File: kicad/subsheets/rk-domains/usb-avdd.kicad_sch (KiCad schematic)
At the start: 16 parts, among them U5 RK3566

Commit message: Mark as R1.0
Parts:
- renumbered C123 to C104, C122 to C105, C121 to C106, C124 to C107, C125 to C108, C155 to C109, C116 to C110, C117 to C111, C118 to C112, R44 to R38, R42 to R39, R43 to R40, R39 to R41, R40 to R42, R41 to R43
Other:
- company: (none) -> UVic Rocketry
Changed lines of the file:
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@@
 	(title_block
 		(title "USB AVDD")
+		(date "2025-11-23")
+		(rev "1.0")
+		(company "UVic Rocketry")
+		(comment 1 "Author: Eric Handley")
 	)
 	(junction
@@
 		(dnp no)
 		(fields_autoplaced yes)
-		(property "Reference" "#PWR062"
+		(property "Reference" "#PWR075"
 			(at 195.58 128.27 0)
 			(effects
@@
 			(project "srad-camera"
 				(path "/da62c771-e8c9-451f-8df1-ec995aadcb11/279fc251-45a8-41a3-8fcf-5855d7fe07da/ae41bc57-04fb-4570-b431-dc406bf562eb"
-					(reference "#PWR062")
+					(reference "#PWR075")
 					(unit 1)
 				)
@@
 		(dnp no)
 		(fields_autoplaced yes)
-		(property "Reference" "R44"
+		(property "Reference" "R38"
 			(at 215.9 62.23 90)
 			(effects
@@
 			(project "srad-camera"
 				(path "/da62c771-e8c9-451f-8df1-ec995aadcb11/279fc251-45a8-41a3-8fcf-5855d7fe07da/ae41bc57-04fb-4570-b431-dc406bf562eb"
-					(reference "R44")
+					(reference "R38")
 					(unit 1)
 				)
@@
 		(dnp no)
 		(fields_autoplaced yes)
-		(property "Reference" "C121"
+		(property "Reference" "C106"
 			(at 212.598 77.216 0)
 			(effects
@@
 			(project "srad-camera"
 				(path "/da62c771-e8c9-451f-8df1-ec995aadcb11/279fc251-45a8-41a3-8fcf-5855d7fe07da/ae41bc57-04fb-4570-b431-dc406bf562eb"
-					(reference "C121")
+					(reference "C106")
 					(unit 1)
 				)
@@
 		(dnp no)
 		(fields_autoplaced yes)
-		(property "Reference" "C117"
+		(property "Reference" "C111"
 			(at 107.188 117.348 0)
 			(effects
@@
 			(project "srad-camera"
 				(path "/da62c771-e8c9-451f-8df1-ec995aadcb11/279fc251-45a8-41a3-8fcf-5855d7fe07da/ae41bc57-04fb-4570-b431-dc406bf562eb"
-					(reference "C117")
+					(reference "C111")
 					(unit 1)
 				)
@@
 		(on_board yes)
 		(dnp no)
-		(property "Reference" "#PWR089"
+		(property "Reference" "#PWR074"
 			(at 81.28 101.6 0)
 			(effects
@@
 			(project "srad-camera"
 				(path "/da62c771-e8c9-451f-8df1-ec995aadcb11/279fc251-45a8-41a3-8fcf-5855d7fe07da/ae41bc57-04fb-4570-b431-dc406bf562eb"
-					(reference "#PWR089")
+					(reference "#PWR074")
 					(unit 1)
 				)
@@
 		(dnp no)
 		(fields_autoplaced yes)
-		(property "Reference" "#PWR061"
+		(property "Reference" "#PWR076"
 			(at 102.87 129.54 0)
 			(effects
@@
 			(project "srad-camera"
 				(path "/da62c771-e8c9-451f-8df1-ec995aadcb11/279fc251-45a8-41a3-8fcf-5855d7fe07da/ae41bc57-04fb-4570-b431-dc406bf562eb"
-					(reference "#PWR061")
+					(reference "#PWR076")
 					(unit 1)
 				)
@@
 		(on_board yes)
 		(dnp no)
-		(property "Reference" "C123"
+		(property "Reference" "C104"
 			(at 201.676 70.104 0)
 			(effects
@@
 			(project "srad-camera"
 				(path "/da62c771-e8c9-451f-8df1-ec995aadcb11/279fc251-45a8-41a3-8fcf-5855d7fe07da/ae41bc57-04fb-4570-b431-dc406bf562eb"
-					(reference "C123")
+					(reference "C104")
 					(unit 1)
 				)
@@
 		(dnp no)
 		(fields_autoplaced yes)
-		(property "Reference" "C118"
+		(property "Reference" "C112"
 			(at 197.612 117.094 0)
 			(effects
@@
 			(project "srad-camera"
 				(path "/da62c771-e8c9-451f-8df1-ec995aadcb11/279fc251-45a8-41a3-8fcf-5855d7fe07da/ae41bc57-04fb-4570-b431-dc406bf562eb"
-					(reference "C118")
+					(reference "C112")
 					(unit 1)
 				)
@@
 		(dnp no)
 		(fields_autoplaced yes)
-		(property "Reference" "#PWR064"
+		(property "Reference" "#PWR072"
 			(at 212.09 86.36 0)
 			(effects
@@
 			(project "srad-camera"
 				(path "/da62c771-e8c9-451f-8df1-ec995aadcb11/279fc251-45a8-41a3-8fcf-5855d7fe07da/ae41bc57-04fb-4570-b431-dc406bf562eb"
-					(reference "#PWR064")
+					(reference "#PWR072")
 					(unit 1)
 				)
@@
 		(on_board yes)
 		(dnp no)
-		(property "Reference" "R39"
+		(property "Reference" "R41"
 			(at 94.488 110.744 90)
 			(effects
@@
 			(project "srad-camera"
 				(path "/da62c771-e8c9-451f-8df1-ec995aadcb11/279fc251-45a8-41a3-8fcf-5855d7fe07da/ae41bc57-04fb-4570-b431-dc406bf562eb"
-					(reference "R39")
+					(reference "R41")
 					(unit 1)
 				)
@@
 		(on_board yes)
 		(dnp no)
-		(property "Reference" "R41"
+		(property "Reference" "R43"
 			(at 200.66 110.49 90)
 			(effects
@@
 			(project "srad-camera"
 				(path "/da62c771-e8c9-451f-8df1-ec995aadcb11/279fc251-45a8-41a3-8fcf-5855d7fe07da/ae41bc57-04fb-4570-b431-dc406bf562eb"
-					(reference "R41")
+					(reference "R43")
 					(unit 1)
 				)
@@
 		(on_board yes)
 		(dnp no)
-		(property "Reference" "C155"
+		(property "Reference" "C109"
 			(at 88.646 104.2557 90)
 			(effects
@@
 			(project "srad-camera"
 				(path "/da62c771-e8c9-451f-8df1-ec995aadcb11/279fc251-45a8-41a3-8fcf-5855d7fe07da/ae41bc57-04fb-4570-b431-dc406bf562eb"
-					(reference "C155")
+					(reference "C109")
 					(unit 1)
 				)
@@
 		(on_board yes)
 		(dnp no)
-		(property "Reference" "C122"
+		(property "Reference" "C105"
 			(at 205.486 80.264 0)
 			(effects
@@
 			(project "srad-camera"
 				(path "/da62c771-e8c9-451f-8df1-ec995aadcb11/279fc251-45a8-41a3-8fcf-5855d7fe07da/ae41bc57-04fb-4570-b431-dc406bf562eb"
-					(reference "C122")
+					(reference "C105")
 					(unit 1)
 				)
@@
 		(dnp no)
 		(fields_autoplaced yes)
-		(property "Reference" "R42"
+		(property "Reference" "R39"
 			(at 211.328 67.564 90)
 			(effects
@@
 			(project "srad-camera"
 				(path "/da62c771-e8c9-451f-8df1-ec995aadcb11/279fc251-45a8-41a3-8fcf-5855d7fe07da/ae41bc57-04fb-4570-b431-dc406bf562eb"
-					(reference "R42")
+					(reference "R39")
 					(unit 1)
 				)
@@
 		(dnp no)
 		(fields_autoplaced yes)
-		(property "Reference" "#PWR065"
+		(property "Reference" "#PWR073"
 			(at 212.09 104.14 0)
 			(effects
@@
 			(project "srad-camera"
 				(path "/da62c771-e8c9-451f-8df1-ec995aadcb11/279fc251-45a8-41a3-8fcf-5855d7fe07da/ae41bc57-04fb-4570-b431-dc406bf562eb"
-					(reference "#PWR065")
+					(reference "#PWR073")
 					(unit 1)
 				)
@@
 		(on_board yes)
 		(dnp no)
-		(property "Reference" "C125"
+		(property "Reference" "C108"
 			(at 213.868 91.948 0)
 			(effects
@@
 			(project "srad-camera"
 				(path "/da62c771-e8c9-451f-8df1-ec995aadcb11/279fc251-45a8-41a3-8fcf-5855d7fe07da/ae41bc57-04fb-4570-b431-dc406bf562eb"
-					(reference "C125")
+					(reference "C108")
 					(unit 1)
 				)
@@
 		(on_board yes)
 		(dnp no)
-		(property "Reference" "R40"
+		(property "Reference" "R42"
 			(at 88.9 116.586 90)
 			(effects
@@
 			(project "srad-camera"
 				(path "/da62c771-e8c9-451f-8df1-ec995aadcb11/279fc251-45a8-41a3-8fcf-5855d7fe07da/ae41bc57-04fb-4570-b431-dc406bf562eb"
-					(reference "R40")
+					(reference "R42")
 					(unit 1)
 				)
@@
 		(dnp no)
 		(fields_autoplaced yes)
-		(property "Reference" "R43"
+		(property "Reference" "R40"
 			(at 218.948 73.152 90)
 			(effects
@@
 			(project "srad-camera"
 				(path "/da62c771-e8c9-451f-8df1-ec995aadcb11/279fc251-45a8-41a3-8fcf-5855d7fe07da/ae41bc57-04fb-4570-b431-dc406bf562eb"
-					(reference "R43")
+					(reference "R40")
 					(unit 1)
 				)
@@
 		(dnp no)
 		(fields_autoplaced yes)
-		(property "Reference" "C116"
+		(property "Reference" "C110"
 			(at 98.552 121.412 0)
 			(effects
@@
 			(project "srad-camera"
 				(path "/da62c771-e8c9-451f-8df1-ec995aadcb11/279fc251-45a8-41a3-8fcf-5855d7fe07da/ae41bc57-04fb-4570-b431-dc406bf562eb"
-					(reference "C116")
+					(reference "C110")
 					(unit 1)
 				)
@@
 		(on_board yes)
 		(dnp no)
-		(property "Reference" "C124"
+		(property "Reference" "C107"
 			(at 205.232 91.948 0)
 			(effects
@@
 			(project "srad-camera"
 				(path "/da62c771-e8c9-451f-8df1-ec995aadcb11/279fc251-45a8-41a3-8fcf-5855d7fe07da/ae41bc57-04fb-4570-b431-dc406bf562eb"
-					(reference "C124")
+					(reference "C107")
 					(unit 1)
 				)

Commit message: Annotations
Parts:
- renumbered C104 to C117, C105 to C118, C106 to C119, C107 to C120, C108 to C121, C109 to C122, C110 to C123, C111 to C124, C112 to C125, R38 to R41, R39 to R42, R40 to R43, R41 to R44, R42 to R45, R43 to R46
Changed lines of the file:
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@@
 		(dnp no)
 		(fields_autoplaced yes)
-		(property "Reference" "#PWR075"
+		(property "Reference" "#PWR085"
 			(at 195.58 128.27 0)
 			(effects
@@
 			(project "srad-camera"
 				(path "/da62c771-e8c9-451f-8df1-ec995aadcb11/279fc251-45a8-41a3-8fcf-5855d7fe07da/ae41bc57-04fb-4570-b431-dc406bf562eb"
-					(reference "#PWR075")
+					(reference "#PWR085")
 					(unit 1)
 				)
@@
 		(dnp no)
 		(fields_autoplaced yes)
-		(property "Reference" "R38"
+		(property "Reference" "R41"
 			(at 215.9 62.23 90)
 			(effects
@@
 			(project "srad-camera"
 				(path "/da62c771-e8c9-451f-8df1-ec995aadcb11/279fc251-45a8-41a3-8fcf-5855d7fe07da/ae41bc57-04fb-4570-b431-dc406bf562eb"
-					(reference "R38")
+					(reference "R41")
 					(unit 1)
 				)
@@
 		(dnp no)
 		(fields_autoplaced yes)
-		(property "Reference" "C106"
+		(property "Reference" "C119"
 			(at 212.598 77.216 0)
 			(effects
@@
 			(project "srad-camera"
 				(path "/da62c771-e8c9-451f-8df1-ec995aadcb11/279fc251-45a8-41a3-8fcf-5855d7fe07da/ae41bc57-04fb-4570-b431-dc406bf562eb"
-					(reference "C106")
+					(reference "C119")
 					(unit 1)
 				)
@@
 		(dnp no)
 		(fields_autoplaced yes)
-		(property "Reference" "C111"
+		(property "Reference" "C124"
 			(at 107.188 117.348 0)
 			(effects
@@
 			(project "srad-camera"
 				(path "/da62c771-e8c9-451f-8df1-ec995aadcb11/279fc251-45a8-41a3-8fcf-5855d7fe07da/ae41bc57-04fb-4570-b431-dc406bf562eb"
-					(reference "C111")
+					(reference "C124")
 					(unit 1)
 				)
@@
 		(on_board yes)
 		(dnp no)
-		(property "Reference" "#PWR074"
+		(property "Reference" "#PWR084"
 			(at 81.28 101.6 0)
 			(effects
@@
 			(project "srad-camera"
 				(path "/da62c771-e8c9-451f-8df1-ec995aadcb11/279fc251-45a8-41a3-8fcf-5855d7fe07da/ae41bc57-04fb-4570-b431-dc406bf562eb"
-					(reference "#PWR074")
+					(reference "#PWR084")
 					(unit 1)
 				)
@@
 		(dnp no)
 		(fields_autoplaced yes)
-		(property "Reference" "#PWR076"
+		(property "Reference" "#PWR086"
 			(at 102.87 129.54 0)
 			(effects
@@
 			(project "srad-camera"
 				(path "/da62c771-e8c9-451f-8df1-ec995aadcb11/279fc251-45a8-41a3-8fcf-5855d7fe07da/ae41bc57-04fb-4570-b431-dc406bf562eb"
-					(reference "#PWR076")
+					(reference "#PWR086")
 					(unit 1)
 				)
@@
 		(on_board yes)
 		(dnp no)
-		(property "Reference" "C104"
+		(property "Reference" "C117"
 			(at 201.676 70.104 0)
 			(effects
@@
 			(project "srad-camera"
 				(path "/da62c771-e8c9-451f-8df1-ec995aadcb11/279fc251-45a8-41a3-8fcf-5855d7fe07da/ae41bc57-04fb-4570-b431-dc406bf562eb"
-					(reference "C104")
+					(reference "C117")
 					(unit 1)
 				)
@@
 		(dnp no)
 		(fields_autoplaced yes)
-		(property "Reference" "C112"
+		(property "Reference" "C125"
 			(at 197.612 117.094 0)
 			(effects
@@
 			(project "srad-camera"
 				(path "/da62c771-e8c9-451f-8df1-ec995aadcb11/279fc251-45a8-41a3-8fcf-5855d7fe07da/ae41bc57-04fb-4570-b431-dc406bf562eb"
-					(reference "C112")
+					(reference "C125")
 					(unit 1)
 				)
@@
 		(dnp no)
 		(fields_autoplaced yes)
-		(property "Reference" "#PWR072"
+		(property "Reference" "#PWR082"
 			(at 212.09 86.36 0)
 			(effects
@@
 			(project "srad-camera"
 				(path "/da62c771-e8c9-451f-8df1-ec995aadcb11/279fc251-45a8-41a3-8fcf-5855d7fe07da/ae41bc57-04fb-4570-b431-dc406bf562eb"
-					(reference "#PWR072")
+					(reference "#PWR082")
 					(unit 1)
 				)
@@
 		(on_board yes)
 		(dnp no)
-		(property "Reference" "R41"
+		(property "Reference" "R44"
 			(at 94.488 110.744 90)
 			(effects
@@
 			(project "srad-camera"
 				(path "/da62c771-e8c9-451f-8df1-ec995aadcb11/279fc251-45a8-41a3-8fcf-5855d7fe07da/ae41bc57-04fb-4570-b431-dc406bf562eb"
-					(reference "R41")
+					(reference "R44")
 					(unit 1)
 				)
@@
 		(on_board yes)
 		(dnp no)
-		(property "Reference" "R43"
+		(property "Reference" "R46"
 			(at 200.66 110.49 90)
 			(effects
@@
 			(project "srad-camera"
 				(path "/da62c771-e8c9-451f-8df1-ec995aadcb11/279fc251-45a8-41a3-8fcf-5855d7fe07da/ae41bc57-04fb-4570-b431-dc406bf562eb"
-					(reference "R43")
+					(reference "R46")
 					(unit 1)
 				)
@@
 		(on_board yes)
 		(dnp no)
-		(property "Reference" "C109"
+		(property "Reference" "C122"
 			(at 88.646 104.2557 90)
 			(effects
@@
 			(project "srad-camera"
 				(path "/da62c771-e8c9-451f-8df1-ec995aadcb11/279fc251-45a8-41a3-8fcf-5855d7fe07da/ae41bc57-04fb-4570-b431-dc406bf562eb"
-					(reference "C109")
+					(reference "C122")
 					(unit 1)
 				)
@@
 		(on_board yes)
 		(dnp no)
-		(property "Reference" "C105"
+		(property "Reference" "C118"
 			(at 205.486 80.264 0)
 			(effects
@@
 			(project "srad-camera"
 				(path "/da62c771-e8c9-451f-8df1-ec995aadcb11/279fc251-45a8-41a3-8fcf-5855d7fe07da/ae41bc57-04fb-4570-b431-dc406bf562eb"
-					(reference "C105")
+					(reference "C118")
 					(unit 1)
 				)
@@
 		(dnp no)
 		(fields_autoplaced yes)
-		(property "Reference" "R39"
+		(property "Reference" "R42"
 			(at 211.328 67.564 90)
 			(effects
@@
 			(project "srad-camera"
 				(path "/da62c771-e8c9-451f-8df1-ec995aadcb11/279fc251-45a8-41a3-8fcf-5855d7fe07da/ae41bc57-04fb-4570-b431-dc406bf562eb"
-					(reference "R39")
+					(reference "R42")
 					(unit 1)
 				)
@@
 		(dnp no)
 		(fields_autoplaced yes)
-		(property "Reference" "#PWR073"
+		(property "Reference" "#PWR083"
 			(at 212.09 104.14 0)
 			(effects
@@
 			(project "srad-camera"
 				(path "/da62c771-e8c9-451f-8df1-ec995aadcb11/279fc251-45a8-41a3-8fcf-5855d7fe07da/ae41bc57-04fb-4570-b431-dc406bf562eb"
-					(reference "#PWR073")
+					(reference "#PWR083")
 					(unit 1)
 				)
@@
 		(on_board yes)
 		(dnp no)
-		(property "Reference" "C108"
+		(property "Reference" "C121"
 			(at 213.868 91.948 0)
 			(effects
@@
 			(project "srad-camera"
 				(path "/da62c771-e8c9-451f-8df1-ec995aadcb11/279fc251-45a8-41a3-8fcf-5855d7fe07da/ae41bc57-04fb-4570-b431-dc406bf562eb"
-					(reference "C108")
+					(reference "C121")
 					(unit 1)
 				)
@@
 		(on_board yes)
 		(dnp no)
-		(property "Reference" "R42"
+		(property "Reference" "R45"
 			(at 88.9 116.586 90)
 			(effects
@@
 			(project "srad-camera"
 				(path "/da62c771-e8c9-451f-8df1-ec995aadcb11/279fc251-45a8-41a3-8fcf-5855d7fe07da/ae41bc57-04fb-4570-b431-dc406bf562eb"
-					(reference "R42")
+					(reference "R45")
 					(unit 1)
 				)
@@
 		(dnp no)
 		(fields_autoplaced yes)
-		(property "Reference" "R40"
+		(property "Reference" "R43"
 			(at 218.948 73.152 90)
 			(effects
@@
 			(project "srad-camera"
 				(path "/da62c771-e8c9-451f-8df1-ec995aadcb11/279fc251-45a8-41a3-8fcf-5855d7fe07da/ae41bc57-04fb-4570-b431-dc406bf562eb"
-					(reference "R40")
+					(reference "R43")
 					(unit 1)
 				)
@@
 		(dnp no)
 		(fields_autoplaced yes)
-		(property "Reference" "C110"
+		(property "Reference" "C123"
 			(at 98.552 121.412 0)
 			(effects
@@
 			(project "srad-camera"
 				(path "/da62c771-e8c9-451f-8df1-ec995aadcb11/279fc251-45a8-41a3-8fcf-5855d7fe07da/ae41bc57-04fb-4570-b431-dc406bf562eb"
-					(reference "C110")
+					(reference "C123")
 					(unit 1)
 				)
@@
 		(on_board yes)
 		(dnp no)
-		(property "Reference" "C107"
+		(property "Reference" "C120"
 			(at 205.232 91.948 0)
 			(effects
@@
 			(project "srad-camera"
 				(path "/da62c771-e8c9-451f-8df1-ec995aadcb11/279fc251-45a8-41a3-8fcf-5855d7fe07da/ae41bc57-04fb-4570-b431-dc406bf562eb"
-					(reference "C107")
+					(reference "C120")
 					(unit 1)
 				)

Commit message: Start on PCB design
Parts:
- C115: renamed from C117; footprint (none) -> Capacitor_SMD:C_0402_1005Metric; LCSC PART NAME (none) -> C1525
- C116: renamed from C118; footprint (none) -> Capacitor_SMD:C_0402_1005Metric; LCSC PART NAME (none) -> C1525
- C117: renamed from C119; footprint (none) -> Capacitor_SMD:C_0402_1005Metric; LCSC PART NAME (none) -> C1525
- C118: renamed from C120; footprint (none) -> Capacitor_SMD:C_0402_1005Metric; LCSC PART NAME (none) -> C1525
- C119: renamed from C121; footprint (none) -> Capacitor_SMD:C_0402_1005Metric; LCSC PART NAME (none) -> C1525
- C120: renamed from C122; footprint (none) -> Capacitor_SMD:C_0402_1005Metric; LCSC PART NAME (none) -> C1525
- C121: renamed from C123; footprint (none) -> Capacitor_SMD:C_0402_1005Metric; LCSC PART NAME (none) -> C1525
- C122: renamed from C124; footprint (none) -> Capacitor_SMD:C_0402_1005Metric; LCSC PART NAME (none) -> C1525
- C123: renamed from C125; footprint (none) -> Capacitor_SMD:C_0402_1005Metric; LCSC PART NAME (none) -> C1525
- R42: renamed from R41; footprint (none) -> Resistor_SMD:R_0402_1005Metric; LCSC PART NAME (none) -> C17168
- R43: renamed from R42; footprint (none) -> Resistor_SMD:R_0402_1005Metric; LCSC PART NAME (none) -> C25086
- R44: renamed from R43; footprint (none) -> Resistor_SMD:R_0402_1005Metric; LCSC PART NAME (none) -> C25086
- R45: renamed from R44; footprint (none) -> Resistor_SMD:R_0402_1005Metric; LCSC PART NAME (none) -> C25086
- R46: renamed from R45; footprint (none) -> Resistor_SMD:R_0402_1005Metric; LCSC PART NAME (none) -> C25086
- R47: renamed from R46; footprint (none) -> Resistor_SMD:R_0402_1005Metric; LCSC PART NAME (none) -> C17168
- U5: LCSC PART NAME RK3566 -> (none)
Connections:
- net USB_DM renamed USB_OTG_DN
- net USB_DP renamed USB_OTG_DP
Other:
- moved on the sheet: C120

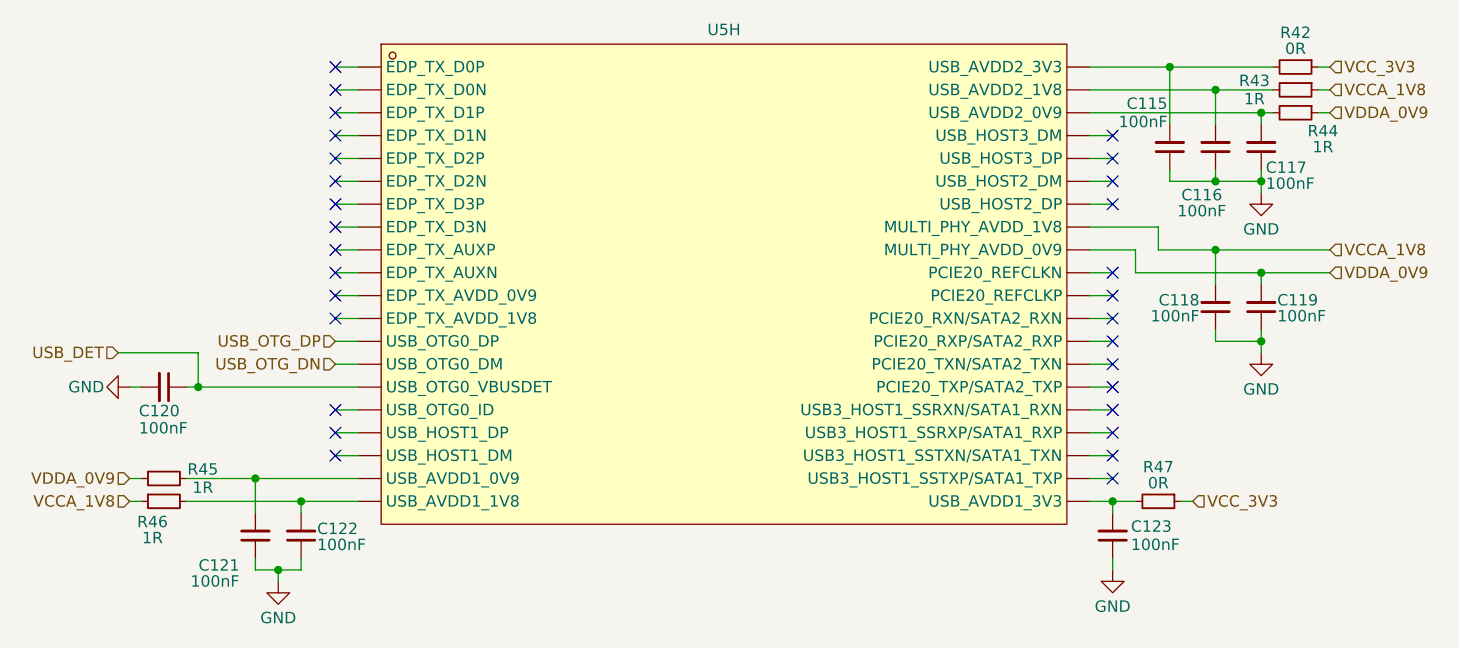
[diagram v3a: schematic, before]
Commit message: Remove power/decoupling for unused power domains
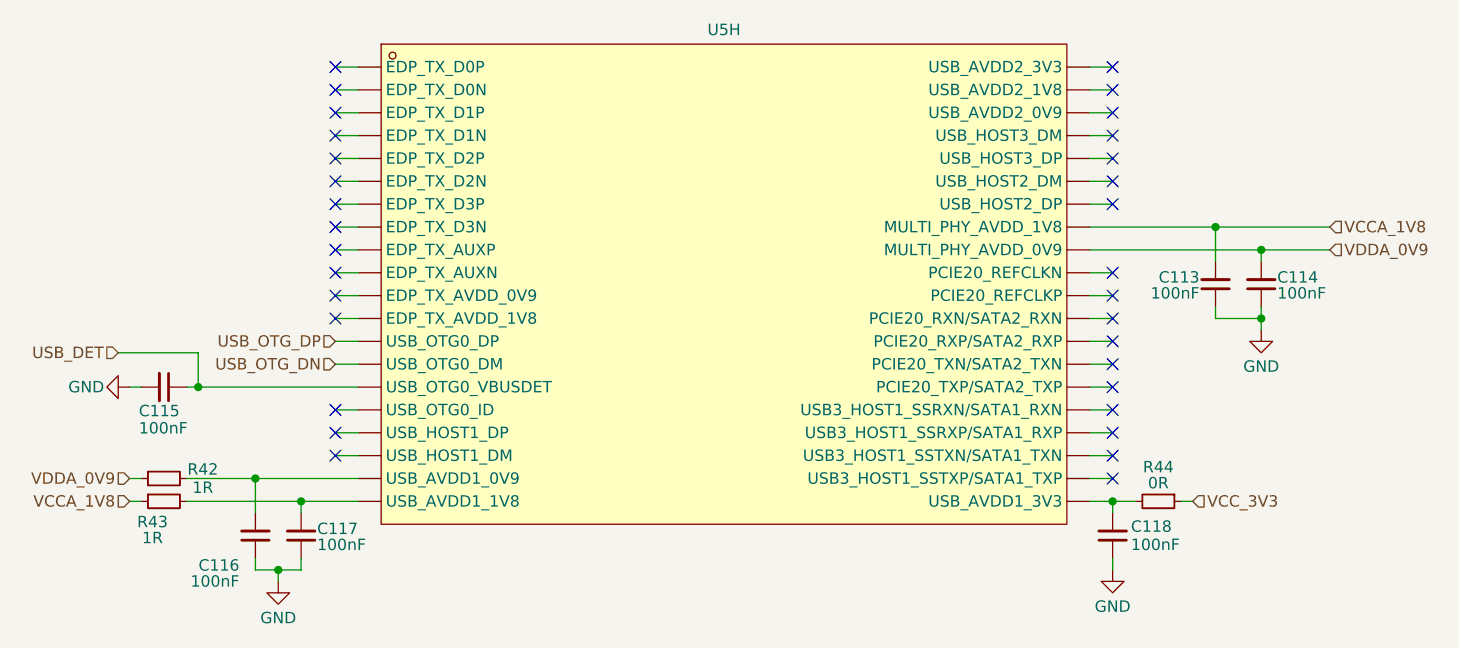
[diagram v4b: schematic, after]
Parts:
- removed C115, C116, C117: 100nF, Capacitor_SMD:C_0402_1005Metric, symbol Device:C_Small
- removed R42: 0R, Resistor_SMD:R_0402_1005Metric, symbol Device:R_Small
- removed R43, R44: 1R, Resistor_SMD:R_0402_1005Metric, symbol Device:R_Small
- renumbered C118 to C113, C119 to C114, C120 to C115, C121 to C116, C122 to C117, C123 to C118, R45 to R42, R46 to R43, R47 to R44
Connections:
- no-connect marks 29 -> 32
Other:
- moved on the sheet: C113, C114
